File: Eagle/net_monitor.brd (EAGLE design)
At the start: 79.7 x 48.2 mm, 15 parts, among them IC1 MCP23008/P

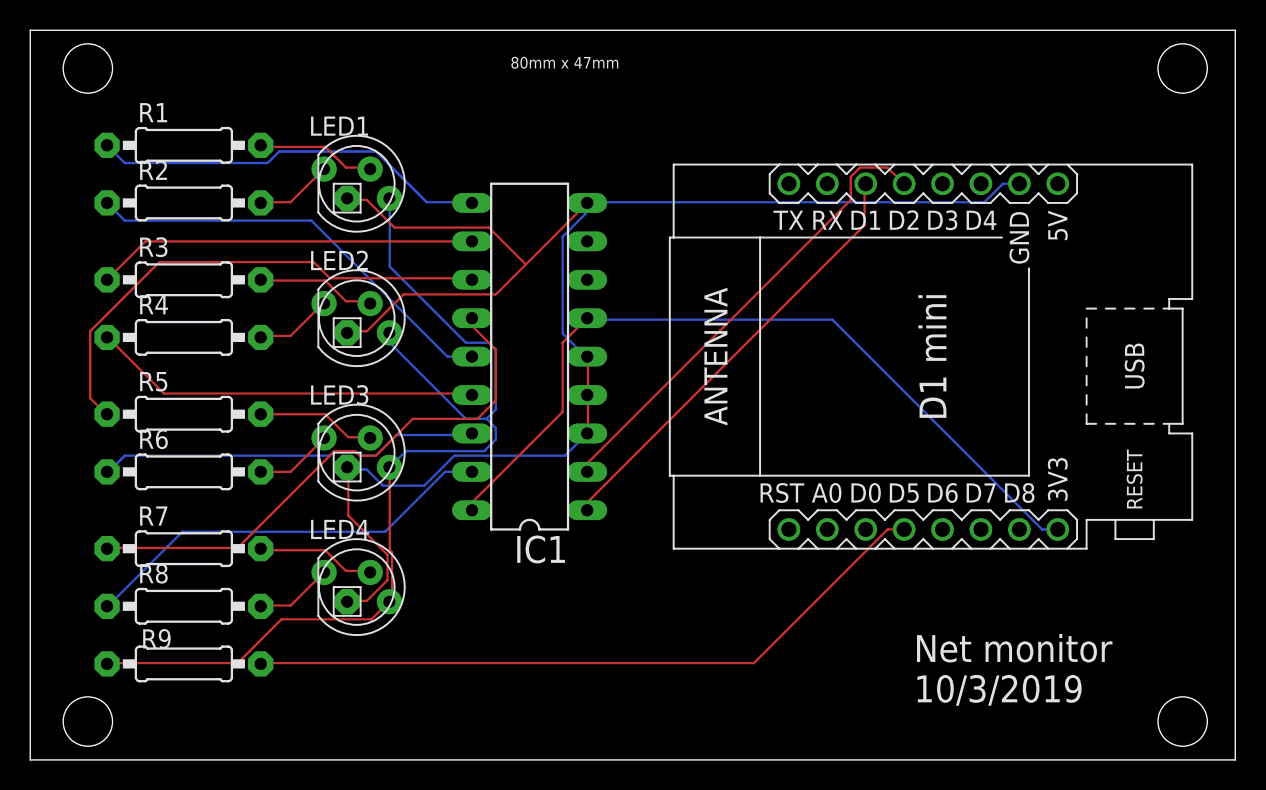
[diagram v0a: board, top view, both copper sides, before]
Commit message: Added a notch in the PCB for the USB connector
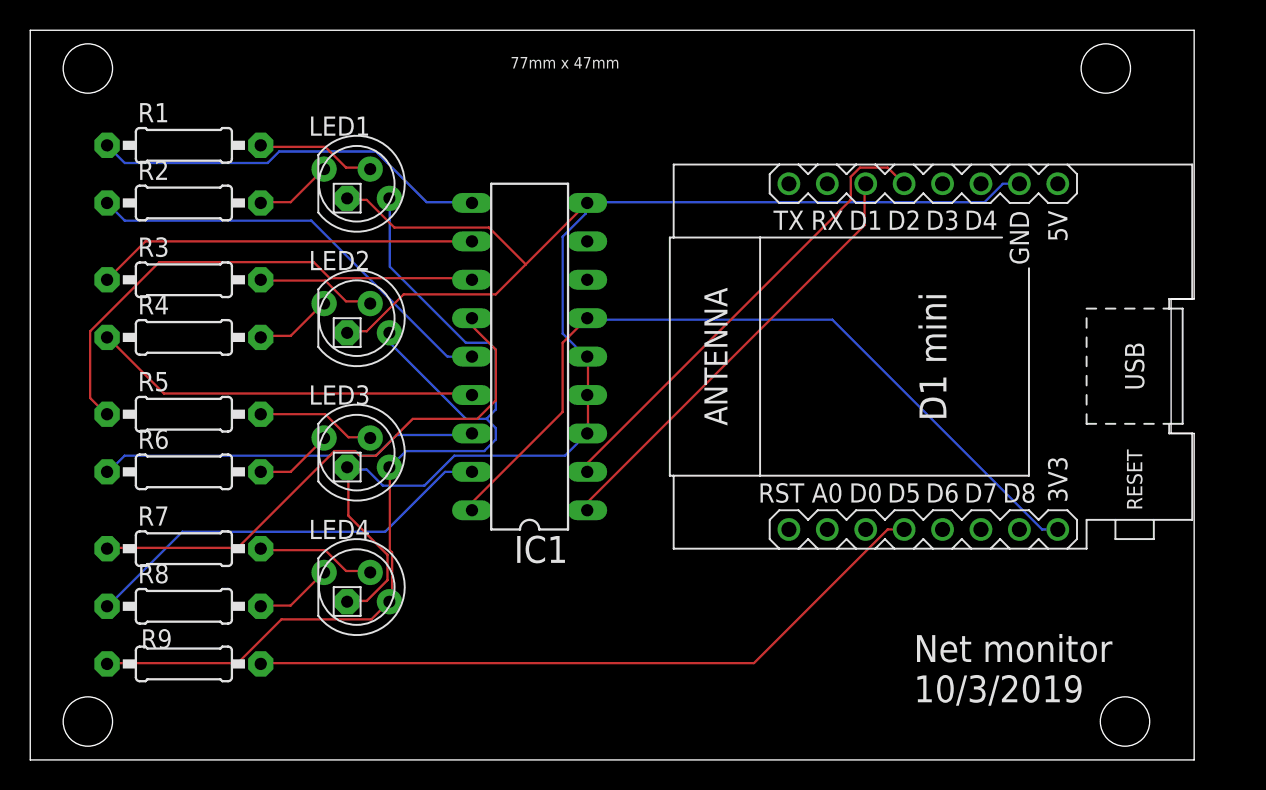
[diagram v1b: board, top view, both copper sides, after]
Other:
- board size 79.7 x 48.2 mm -> 77 x 48.2 mm
- board text added: "77mm x 47mm"
- board text removed: "80mm x 47mm"
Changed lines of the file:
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@@
 <?xml version="1.0" encoding="utf-8"?>
 <!DOCTYPE eagle SYSTEM "eagle.dtd">
-<eagle version="9.3.2">
+<eagle version="9.6.2">
 <drawing>
 <settings>
@@
 <setting verticaltext="up"/>
 </settings>
-<grid distance="50" unitdist="mil" unit="inch" style="lines" multiple="1" display="yes" altdistance="5" altunitdist="mil" altunit="mil"/>
+<grid distance="0.01" unitdist="inch" unit="inch" style="lines" multiple="1" display="yes" altdistance="5" altunitdist="mil" altunit="mil"/>
 <layers>
 <layer number="1" name="Top" color="4" fill="1" visible="yes" active="yes"/>
@@
 <board>
 <plain>
-<wire x1="0" y1="0" x2="79.68" y2="0" width="0" layer="20"/>
-<wire x1="79.68" y1="0" x2="79.68" y2="48.25" width="0" layer="20"/>
-<wire x1="79.68" y1="48.25" x2="0" y2="48.25" width="0" layer="20"/>
+<wire x1="0" y1="0" x2="76.962" y2="0" width="0" layer="20"/>
+<wire x1="76.962" y1="0" x2="76.962" y2="21.59" width="0" layer="20"/>
+<wire x1="76.962" y1="21.59" x2="75.438" y2="21.59" width="0" layer="20"/>
+<wire x1="75.438" y1="21.59" x2="75.438" y2="30.48" width="0" layer="20"/>
+<wire x1="75.438" y1="30.48" x2="76.962" y2="30.48" width="0" layer="20"/>
+<wire x1="76.962" y1="30.48" x2="76.962" y2="48.25" width="0" layer="20"/>
+<wire x1="76.962" y1="48.25" x2="0" y2="48.25" width="0" layer="20"/>
 <wire x1="0" y1="48.25" x2="0" y2="0" width="0" layer="20"/>
 <text x="58.42" y="3.81" size="1.778" layer="21">Net monitor
@@
 <hole x="3.81" y="45.72" drill="3.2639"/>
 <hole x="3.81" y="2.54" drill="3.2639"/>
-<hole x="76.2" y="2.54" drill="3.2639"/>
-<hole x="76.2" y="45.72" drill="3.2639"/>
-<text x="31.75" y="45.72" size="0.762" layer="21">80mm x 47mm</text>
+<hole x="72.39" y="2.54" drill="3.2639"/>
+<hole x="71.12" y="45.72" drill="3.2639"/>
+<text x="31.75" y="45.72" size="0.762" layer="21">77mm x 47mm</text>
 </plain>
 <attributes>
